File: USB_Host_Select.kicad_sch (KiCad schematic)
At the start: 9 parts, among them J10 USB_C_Receptacle_USB2.0_16P, J11 USB_C_Receptacle_USB2.0_16P, U3 TS3USB221AQRSERQ1, U7 USBLC6-2SC6, U8 USBLC6-2SC6

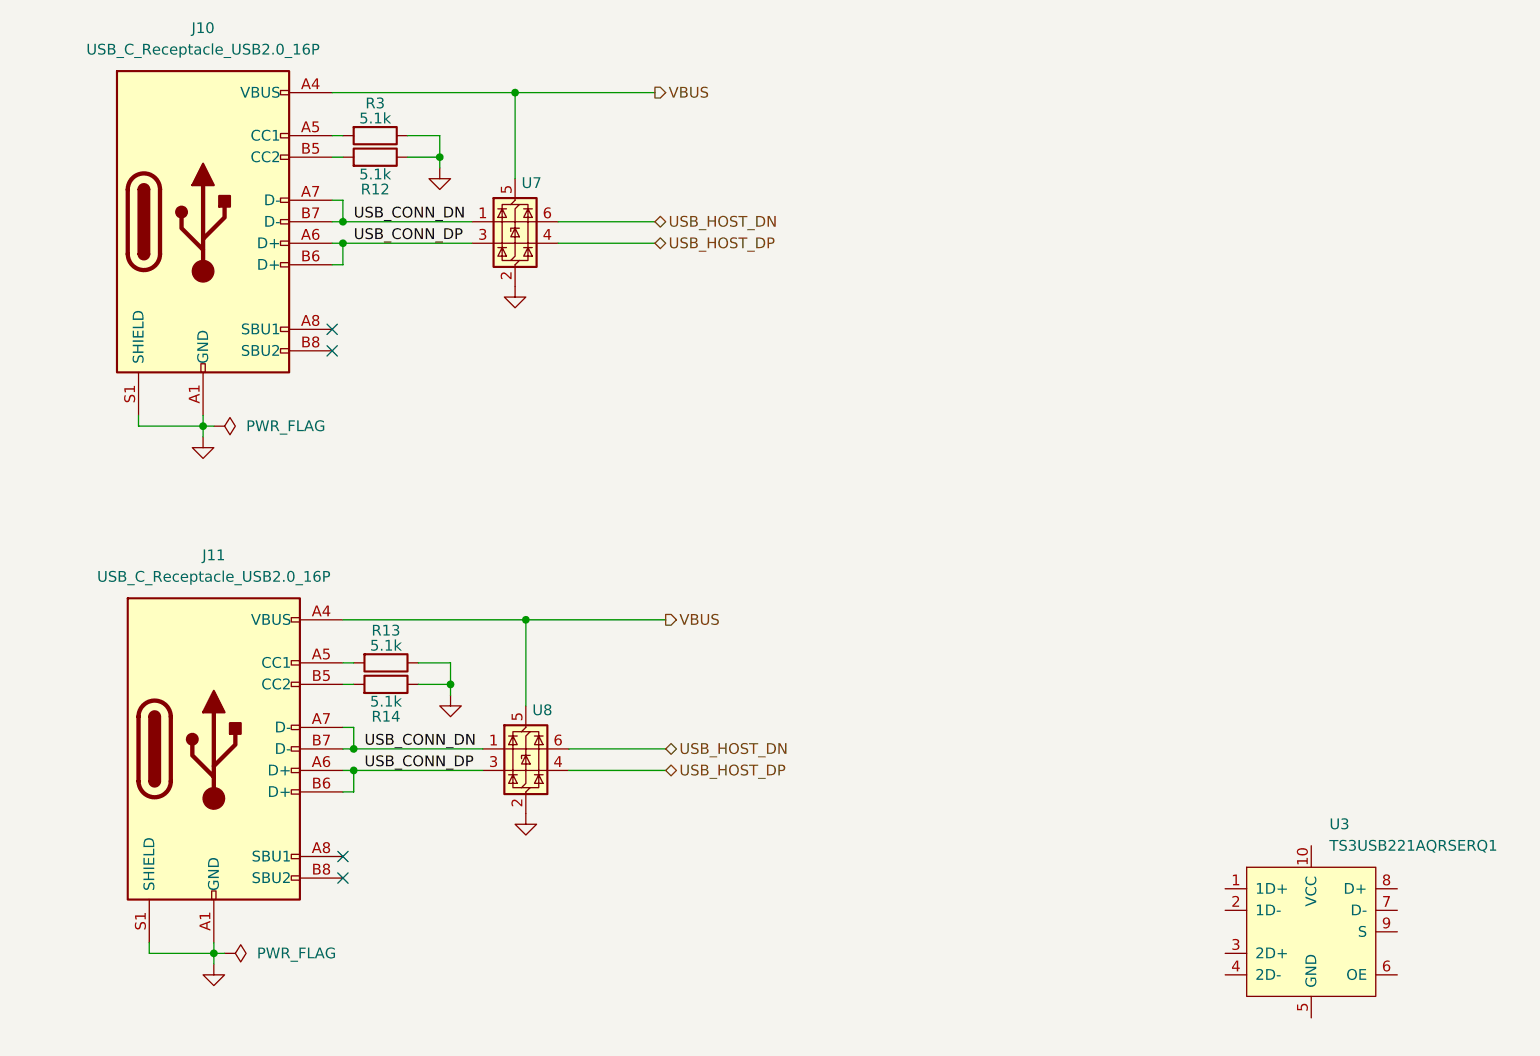
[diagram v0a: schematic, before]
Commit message: Better schematics structure & Hub sub-circuit connections
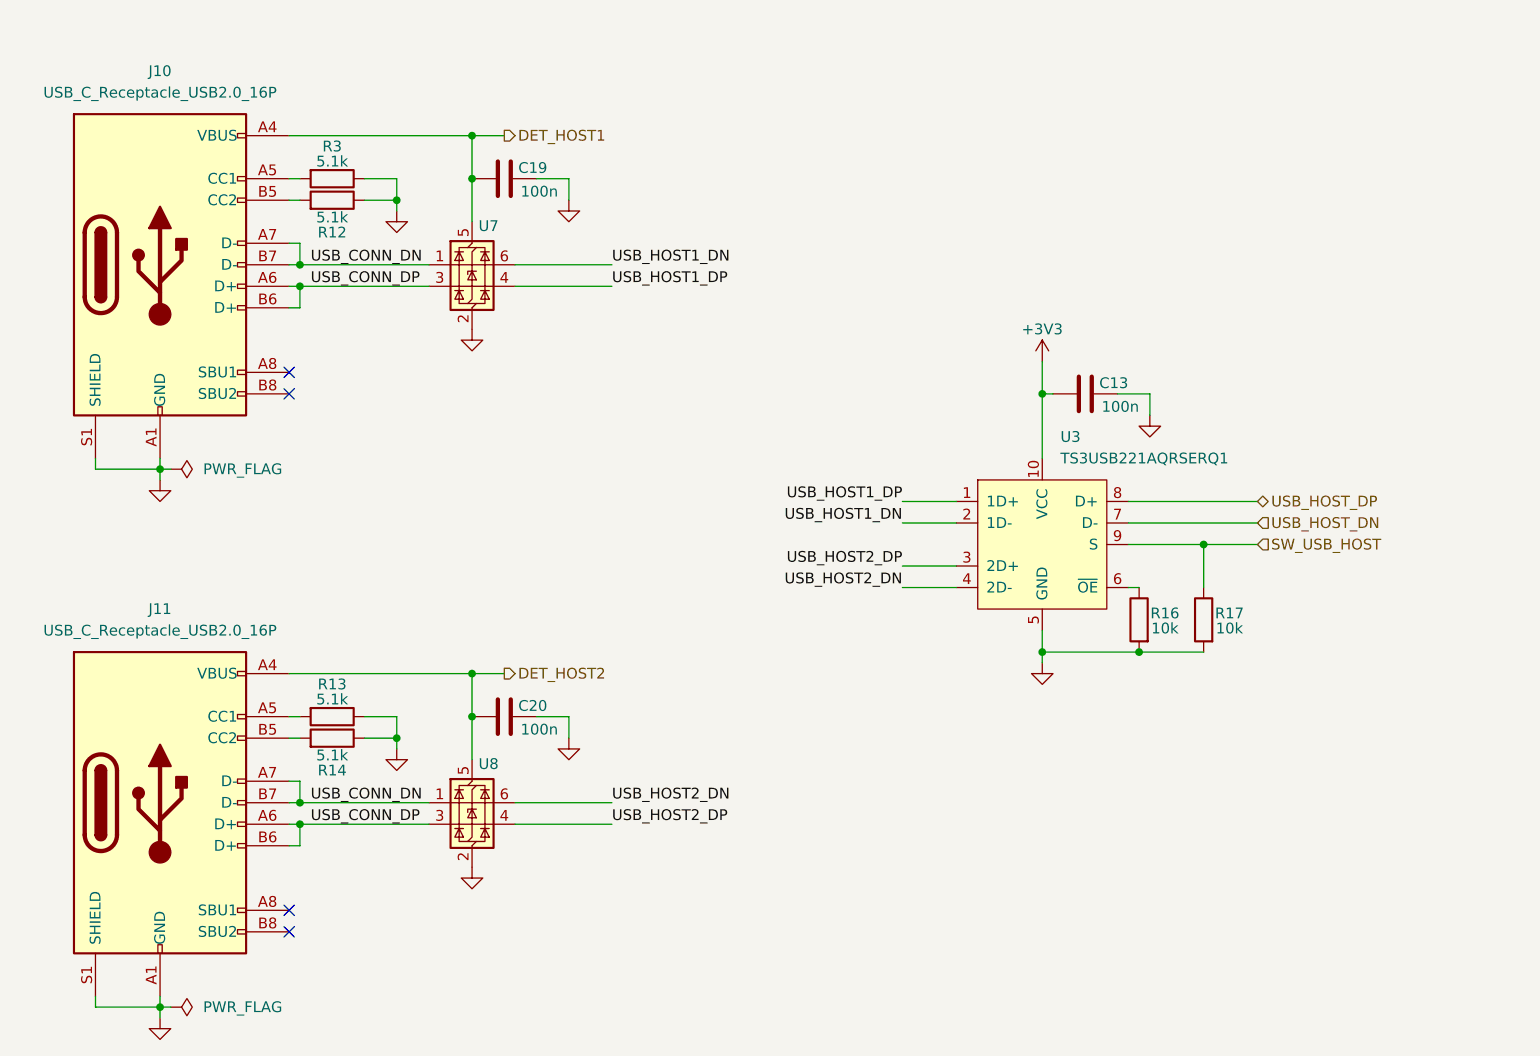
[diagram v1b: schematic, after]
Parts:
- added C13, C19, C20: 100n, Capacitor_SMD:C_0603_1608Metric, symbol Device:C
- added R16, R17: 10k, Resistor_SMD:R_0603_1608Metric, symbol Device:R
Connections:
- net GND: now also U3.5 (GND), C13.2, C19.2, C20.2, R16.2, R17.2
- net USB_HOST_DN: now also U3.7 (D-); no longer U7.6 (I/O1), U8.6 (I/O1)
- net USB_HOST_DP: now also U3.8 (D+); no longer U7.4 (I/O2), U8.4 (I/O2)
- net USB_HOST1_DP: now reaches U3.1 (1D+)
- net USB_HOST1_DP: now also U7.4 (I/O2)
- net +3V3: now reaches U3.10 (VCC)
- net +3V3: now also C13.1
- net USB_HOST1_DN: now reaches U3.2 (1D-)
- net USB_HOST1_DN: now also U7.6 (I/O1)
- net USB_HOST2_DP: now reaches U3.3 (2D+)
- net USB_HOST2_DP: now also U8.4 (I/O2)
- net USB_HOST2_DN: now reaches U3.4 (2D-)
- net USB_HOST2_DN: now also U8.6 (I/O1)
- net at U3.6 (~{OE}): now also R16.1
- net SW_USB_HOST: now reaches U3.9 (S)
- net SW_USB_HOST: now also R17.1
- net VBUS renamed DET_HOST1
- net DET_HOST1: now also C19.1; no longer J11.A4 (VBUS), J11.A9 (VBUS), J11.B4 (VBUS), J11.B9 (VBUS), U8.5 (VBUS)
- new net DET_HOST2: C20.1, J11.A4 (VBUS), J11.A9 (VBUS), J11.B4 (VBUS), J11.B9 (VBUS), U8.5 (VBUS)
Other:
- moved on the sheet: J10, J11, R12, R13, R14, R3, U3, U7, U8

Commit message: Updated symbols' DigiKey part no.
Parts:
- U3: DigiKey (none) -> 296-27719-1-ND
- U7, U8: DigiKey 4518-USBLC6-2SC6CT-ND -> 5399-USBLC6-2SC6CT-ND
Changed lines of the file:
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@@
 			)
 		)
-		(property "DigiKey" "4518-USBLC6-2SC6CT-ND"
+		(property "DigiKey" "5399-USBLC6-2SC6CT-ND"
 			(at 97.79 132.08 0)
 			(hide yes)
@@
 			)
 		)
-		(property "DigiKey" "4518-USBLC6-2SC6CT-ND"
+		(property "DigiKey" "5399-USBLC6-2SC6CT-ND"
 			(at 97.79 68.58 0)
 			(hide yes)
@@
 			(at 165.1 101.6 0)
 			(hide yes)
+			(show_name no)
+			(do_not_autoplace no)
+			(effects
+				(font
+					(size 1.27 1.27)
+				)
+			)
+		)
+		(property "DigiKey" "296-27719-1-ND"
+			(at 165.1 101.6 0)
+			(hide yes)

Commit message: Changed MCU & Stared routing HDMI connectiors
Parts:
- C14: renamed from C19; AX (none) -> 27012; AX no. 27012 -> (none)
- C15: renamed from C20; AX (none) -> 27012; AX no. 27012 -> (none)
- C16: renamed from C13; AX (none) -> 27012; AX no. 27012 -> (none)
- J2: renamed from J10; Name USB4105-GF-A -> (none)
- J3: renamed from J11; Name USB4105-GF-A -> (none)
- R10: renamed from R3; Name RC0603FR-075K1L -> (none)
- R11: renamed from R12; Name RC0603FR-075K1L -> (none)
- R12: renamed from R13; Name RC0603FR-075K1L -> (none)
- R13: renamed from R14; Name RC0603FR-075K1L -> (none)
- R14: renamed from R16; footprint Resistor_SMD:R_0603_1608Metric -> Resistor_SMD:R_0402_1005Metric; AX (none) -> 201002; AX no. 141002 -> (none)
- R15: renamed from R17; footprint Resistor_SMD:R_0603_1608Metric -> Resistor_SMD:R_0402_1005Metric; AX (none) -> 201002; AX no. 141002 -> (none)
- U4: renamed from U7; Name USBLC6-2SC6 -> (none)
- U5: renamed from U8; Name USBLC6-2SC6 -> (none)
- renumbered U3 to U6

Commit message: HDMI schematics
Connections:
- net SW_USB_HOST renamed SW
- net USB_CONN_DN renamed USB_CONN_A_DN
- net USB_CONN_A_DN: no longer J3.A7 (D-), J3.B7 (D-), U5.1 (I/O1)
- net USB_CONN_DP renamed USB_CONN_A_DP
- net USB_CONN_A_DP: no longer J3.A6 (D+), J3.B6 (D+), U5.3 (I/O2)
- net USB_HOST1_DN renamed USB_A_DN
- net USB_HOST1_DP renamed USB_A_DP
- net USB_HOST2_DN renamed USB_B_DN
- net USB_HOST2_DP renamed USB_B_DP
- new net USB_CONN_B_DN: J3.A7 (D-), J3.B7 (D-), U5.1 (I/O1)
- new net USB_CONN__BDP: J3.A6 (D+), J3.B6 (D+), U5.3 (I/O2)
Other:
- note added: "S LOW => 1D+/- = D+/-"
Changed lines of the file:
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@@
 		(rev "A")
+	)
+	(text "S LOW => 1D+/- = D+/-"
+		(exclude_from_sim no)
+		(at 203.708 106.426 0)
+		(effects
+			(font
+				(size 1.27 1.27)
+			)
+		)
 	)
 	(junction
@@
 	(wire
 		(pts
+			(xy 165.1 80.01) (xy 165.1 83.82)
+		)
+		(stroke
+			(width 0)
+			(type default)
+		)
+	)
+	(wire
+		(pts
+			(xy 77.47 73.66) (xy 76.2 73.66)
+		)
+		(stroke
+			(width 0)
+			(type default)
+		)
+	)
+	(wire
+		(pts
 			(xy 77.47 134.62) (xy 92.71 134.62)
 		)
@@
 	(wire
 		(pts
-			(xy 165.1 80.01) (xy 165.1 83.82)
-		)
-		(stroke
-			(width 0)
-			(type default)
-		)
-	)
-	(wire
-		(pts
-			(xy 77.47 73.66) (xy 76.2 73.66)
-		)
-		(stroke
-			(width 0)
-			(type default)
-		)
-	)
-	(wire
-		(pts
 			(xy 85.09 60.96) (xy 88.9 60.96)
 		)
@@
 		)
 	)
-	(label "USB_HOST1_DP"
+	(label "USB_A_DP"
 		(at 148.59 96.52 180)
 		(effects
@@
 		)
 	)
-	(label "USB_HOST2_DN"
+	(label "USB_B_DN"
 		(at 114.3 132.08 0)
 		(effects
@@
 		)
 	)
-	(label "USB_HOST2_DP"
+	(label "USB_B_DP"
 		(at 114.3 134.62 0)
 		(effects
@@
 		)
 	)
-	(label "USB_CONN_DN"
-		(at 78.74 68.58 0)
+	(label "USB_CONN_A_DN"
+		(at 77.47 68.58 0)
 		(effects
 			(font
@@
 		)
 	)
-	(label "USB_HOST1_DN"
+	(label "USB_A_DN"
 		(at 114.3 68.58 0)
 		(effects
@@
 		)
 	)
-	(label "USB_CONN_DP"
-		(at 78.74 134.62 0)
+	(label "USB_CONN__BDP"
+		(at 77.47 134.62 0)
 		(effects
 			(font
@@
 		)
 	)
-	(label "USB_HOST2_DN"
+	(label "USB_B_DN"
 		(at 148.59 106.68 180)
 		(effects
@@
 		)
 	)
-	(label "USB_HOST1_DN"
+	(label "USB_A_DN"
 		(at 148.59 99.06 180)
 		(effects
@@
 		)
 	)
-	(label "USB_HOST1_DP"
+	(label "USB_A_DP"
 		(at 114.3 71.12 0)
 		(effects
@@
 		)
 	)
-	(label "USB_HOST2_DP"
+	(label "USB_B_DP"
 		(at 148.59 104.14 180)
 		(effects
@@
 		)
 	)
-	(label "USB_CONN_DN"
-		(at 78.74 132.08 0)
+	(label "USB_CONN_B_DN"
+		(at 77.47 132.08 0)
 		(effects
 			(font
@@
 		)
 	)
-	(label "USB_CONN_DP"
-		(at 78.74 71.12 0)
+	(label "USB_CONN_A_DP"
+		(at 77.47 71.12 0)
 		(effects
 			(font
@@
 		)
 	)
-	(hierarchical_label "SW_USB_HOST"
+	(hierarchical_label "SW"
 		(shape input)
 		(at 190.5 101.6 0)

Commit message: Schematics done
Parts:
- removed C14, C15, C16: 100n, Capacitor_SMD:C_0603_1608Metric, symbol Device:C
- added C28, C30, C31: 1u, Capacitor_SMD:C_0402_1005Metric, symbol Device:C
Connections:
- net +3V3: now also C28.1
- net GND: now also C28.2, C30.2, C31.2
- net DET_HOST1: no longer names the net of J2.A4 (VBUS), J2.A9 (VBUS), J2.B4 (VBUS), J2.B9 (VBUS), U4.5 (VBUS)
- net DET_HOST1: now also C30.1
- net DET_HOST2: no longer names the net of J3.A4 (VBUS), J3.A9 (VBUS), J3.B4 (VBUS), J3.B9 (VBUS), U5.5 (VBUS)
- net DET_HOST2: now also C31.1
- net USB_HOST_DN renamed USB_UP_DN
- net USB_HOST_DP renamed USB_UP_DP

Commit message: Fixed DRC & Adnotations
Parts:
- renumbered C30 to C1, C28 to C2, C31 to C3, J2 to J1, J3 to J2, R10 to R1, R11 to R2, R14 to R3, R15 to R4, R12 to R5, R13 to R6, U4 to U1, U6 to U2, U5 to U3
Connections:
- net GND: now also J1.SH (SHIELD), J2.SH (SHIELD); no longer J1.S1 (SHIELD), J2.S1 (SHIELD)

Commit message: Updated library structure
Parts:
- removed U2: TS3USB221AQRSERQ1, TS3USB221AQRSERQ1:TS3USB221AQRSERQ1, symbol TS3USB221AQRSERQ1:TS3USB221AQRSERQ1
- added U2: TS3USB221AQRSERQ1, TS3USB221AQRSERQ1:TS3USB221AQRSERQ1, symbol Symbols:TS3USB221AQRSERQ1
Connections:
- net +3V3: now also U2.10 (VCC)
- net GND: now also U2.5 (GND)
- net SW: now also U2.9 (S)
- net USB_A_DN: now also U2.2 (1D-)
- net USB_A_DP: now also U2.1 (1D+)
- net USB_B_DN: now also U2.4 (2D-)
- net USB_B_DP: now also U2.3 (2D+)
- net USB_UP_DN: now also U2.7 (D-)
- net USB_UP_DP: now also U2.8 (D+)
- net at R3.1: now also U2.6 (~{OE})
- net USB_CONN__BDP renamed USB_CONN_B_DP
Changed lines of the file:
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@@
 		)
 	)
-	(label "USB_CONN__BDP"
+	(label "USB_CONN_B_DP"
 		(at 77.47 134.62 0)
 		(effects
@@
 	)
 	(symbol
+		(lib_id "Symbols:TS3USB221AQRSERQ1")
+		(at 165.1 101.6 0)
+		(unit 1)
+		(body_style 1)
+		(exclude_from_sim no)
+		(in_bom yes)
+		(on_board yes)
+		(in_pos_files yes)
+		(dnp no)
+		(fields_autoplaced yes)
+		(property "Reference" "U2"
+			(at 167.2433 88.9 0)
+			(show_name no)
+			(do_not_autoplace no)
+			(effects
+				(font
+					(size 1.27 1.27)
+				)
+				(justify left)
+			)
+		)
+		(property "Value" "TS3USB221AQRSERQ1"
+			(at 167.2433 91.44 0)
+			(show_name no)
+			(do_not_autoplace no)
+			(effects
+				(font
+					(size 1.27 1.27)
+				)
+				(justify left)
+			)
+		)
+		(property "Footprint" "TS3USB221AQRSERQ1:TS3USB221AQRSERQ1"
+			(at 165.1 101.6 0)
+			(hide yes)
+			(show_name no)
+			(do_not_autoplace no)
+			(effects
+				(font
+					(size 1.27 1.27)
+				)
+			)
+		)
+		(property "Datasheet" "https://www.ti.com/lit/ds/scds300e/scds300e.pdf"
+			(at 165.1 101.6 0)
+			(hide yes)
+			(show_name no)
+			(do_not_autoplace no)
+			(effects
+				(font
+					(size 1.27 1.27)
+				)
+			)
+		)
+		(property "Description" "Automotive ESD protected high-speed USB 2.0 1:2 multiplexer/demultiplexer switch"
+			(at 165.1 101.6 0)
+			(hide yes)
+			(show_name no)
+			(do_not_autoplace no)
+			(effects
+				(font
+					(size 1.27 1.27)
+				)
+			)
+		)
+		(property "DigiKey" "296-27719-1-ND"
+			(at 165.1 101.6 0)
+			(hide yes)
+			(show_name no)
+			(do_not_autoplace no)
+			(effects
+				(font
+					(size 1.27 1.27)
+				)
+			)
+		)
+		(pin "3"
+		)
+		(pin "2"
+		)
+		(pin "1"
+		)
+		(pin "9"
+		)
+		(pin "10"
+		)
+		(pin "6"
+		)
+		(pin "8"
+		)
+		(pin "7"
+		)
+		(pin "5"
+		)
+		(pin "4"
+		)
+		(instances
+			(project "KVM_Switch"
+				(path "/94386106-ccd4-487f-b5c5-d52ec3dd59db/e397aa06-0b86-4196-a73c-4d06e82b65f2"
+					(reference "U2")
+					(unit 1)
+				)
+			)
+		)
+	)
+	(symbol
 		(lib_id "power:GND")
 		(at 88.9 62.23 0)
@@
 					(unit 1)
 				)
-			)
-		)
-	)
-	(symbol
-		(lib_id "TS3USB221AQRSERQ1:TS3USB221AQRSERQ1")
-		(at 165.1 101.6 0)
-		(unit 1)
-		(body_style 1)
-		(exclude_from_sim no)
-		(in_bom yes)
-		(on_board yes)
-		(in_pos_files yes)
-		(dnp no)
-		(fields_autoplaced yes)
-		(property "Reference" "U2"
-			(at 167.2433 88.9 0)
-			(show_name no)
-			(do_not_autoplace no)
-			(effects
-				(font
-					(size 1.27 1.27)
-				)
-				(justify left)
-			)
-		)
-		(property "Value" "TS3USB221AQRSERQ1"
-			(at 167.2433 91.44 0)
-			(show_name no)
-			(do_not_autoplace no)
-			(effects
-				(font
-					(size 1.27 1.27)
-				)
-				(justify left)
-			)
-		)
-		(property "Footprint" "TS3USB221AQRSERQ1:TS3USB221AQRSERQ1"
-			(at 165.1 101.6 0)
-			(hide yes)
-			(show_name no)
-			(do_not_autoplace no)
-			(effects
-				(font
-					(size 1.27 1.27)
-				)
-			)
-		)
-		(property "Datasheet" "https://www.ti.com/lit/ds/scds300e/scds300e.pdf"
-			(at 165.1 101.6 0)
-			(hide yes)
-			(show_name no)
-			(do_not_autoplace no)
-			(effects
-				(font
-					(size 1.27 1.27)
-				)
-			)
-		)
-		(property "Description" "Automotive ESD protected high-speed USB 2.0 1:2 multiplexer/demultiplexer switch"
-			(at 165.1 101.6 0)
-			(hide yes)
-			(show_name no)
-			(do_not_autoplace no)
-			(effects
-				(font
-					(size 1.27 1.27)
-				)
-			)
-		)
-		(property "DigiKey" "296-27719-1-ND"
-			(at 165.1 101.6 0)
-			(hide yes)
-			(show_name no)
-			(do_not_autoplace no)
-			(effects
-				(font
-					(size 1.27 1.27)
-				)
-			)
-		)
-		(pin "9"
-		)
-		(pin "8"
-		)
-		(pin "7"
-		)
-		(pin "6"
-		)
-		(pin "5"
-		)
-		(pin "4"
-		)
-		(pin "3"
-		)
-		(pin "2"
-		)
-		(pin "1"
-		)
-		(pin "10"
-		)
-		(instances
-			(project "KVM_Switch"
-				(path "/94386106-ccd4-487f-b5c5-d52ec3dd59db/e397aa06-0b86-4196-a73c-4d06e82b65f2"
-					(reference "U2")
-					(unit 1)
-				)

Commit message: Library and Schematics Fixes
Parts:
- removed R4: 10k, Resistor_SMD:R_0402_1005Metric, symbol Device:R
- U2: footprint TS3USB221AQRSERQ1:TS3USB221AQRSERQ1 -> KVM_Swtich:TS3USB221AQRSERQ1
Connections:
- net DET_USB_B: now reaches C3.1, J2.A4 (VBUS), J2.A9 (VBUS), J2.B4 (VBUS), J2.B9 (VBUS), U3.5 (VBUS)
- net DET_USB_A: now reaches C1.1, J1.A4 (VBUS), J1.A9 (VBUS), J1.B4 (VBUS), J1.B9 (VBUS), U1.5 (VBUS)
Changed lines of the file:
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@@
-	)
-	(junction
-		(at 176.53 114.3)
-		(diameter 0)
-		(color 0 0 0 0)
 	)
 	(junction
@@
 	)
 	(junction
-		(at 184.15 101.6)
+		(at 107.95 53.34)
 		(diameter 0)
 		(color 0 0 0 0)
@@
 		(color 0 0 0 0)
 	)
+	(junction
+		(at 107.95 116.84)
+		(diameter 0)
+		(color 0 0 0 0)
+	)
 	(no_connect
 		(at 76.2 144.78)
@@
 	(wire
 		(pts
-			(xy 184.15 101.6) (xy 190.5 101.6)
-		)
-		(stroke
-			(width 0)
-			(type default)
-		)
-	)
-	(wire
-		(pts
 			(xy 76.2 60.96) (xy 77.47 60.96)
 		)
@@
 	(wire
 		(pts
+			(xy 107.95 116.84) (xy 114.3 116.84)
+		)
+		(stroke
+			(width 0)
+			(type default)
+		)
+	)
+	(wire
+		(pts
 			(xy 77.47 71.12) (xy 77.47 73.66)
 		)
@@
 	(wire
 		(pts
-			(xy 176.53 114.3) (xy 184.15 114.3)
-		)
-		(stroke
-			(width 0)
-			(type default)
-		)
-	)
-	(wire
-		(pts
-			(xy 175.26 101.6) (xy 184.15 101.6)
+			(xy 175.26 101.6) (xy 190.5 101.6)
 		)
 		(stroke
@@
 	(wire
 		(pts
+			(xy 107.95 53.34) (xy 114.3 53.34)
+		)
+		(stroke
+			(width 0)
+			(type default)
+		)
+	)
+	(wire
+		(pts
 			(xy 77.47 132.08) (xy 92.71 132.08)
 		)
@@
 		(pts
 			(xy 97.79 116.84) (xy 76.2 116.84)
-		)
-		(stroke
-			(width 0)
-			(type default)
-		)
-	)
-	(wire
-		(pts
-			(xy 184.15 101.6) (xy 184.15 106.68)
 		)
 		(stroke
@@
 			)
 			(justify left bottom)
+		)
+	)
+	(hierarchical_label "DET_USB_B"
+		(shape output)
+		(at 114.3 116.84 0)
+		(effects
+			(font
+				(size 1.27 1.27)
+			)
+			(justify left)
 		)
 	)
@@
 		(shape input)
 		(at 190.5 101.6 0)
+		(effects
+			(font
+				(size 1.27 1.27)
+			)
+			(justify left)
+		)
+	)
+	(hierarchical_label "DET_USB_A"
+		(shape output)
+		(at 114.3 53.34 0)
 		(effects
 			(font
@@
 	)
 	(symbol
-		(lib_id "Device:R")
-		(at 184.15 110.49 0)
-		(mirror y)
-		(unit 1)
-		(body_style 1)
-		(exclude_from_sim no)
-		(in_bom yes)
-		(on_board yes)
-		(in_pos_files yes)
-		(dnp no)
-		(property "Reference" "R4"
-			(at 187.198 109.728 0)
-			(show_name no)
-			(do_not_autoplace no)
-			(effects
-				(font
-					(size 1.27 1.27)
-				)
-			)
-		)
-		(property "Value" "10k"
-			(at 187.198 111.506 0)
-			(show_name no)
-			(do_not_autoplace no)
-			(effects
-				(font
-					(size 1.27 1.27)
-				)
-			)
-		)
-		(property "Footprint" "Resistor_SMD:R_0402_1005Metric"
-			(at 185.928 110.49 90)
-			(hide yes)
-			(show_name no)
-			(do_not_autoplace no)
-			(effects
-				(font
-					(size 1.27 1.27)
-				)
-			)
-		)
-		(property "Datasheet" ""
-			(at 184.15 110.49 0)
-			(hide yes)
-			(show_name no)
-			(do_not_autoplace no)
-			(effects
-				(font
-					(size 1.27 1.27)
-				)
-			)
-		)
-		(property "Description" "Resistor"
-			(at 184.15 110.49 0)
-			(hide yes)
-			(show_name no)
-			(do_not_autoplace no)
-			(effects
-				(font
-					(size 1.27 1.27)
-				)
-			)
-		)
-		(property "AX" "201002"
-			(at 184.15 110.49 0)
-			(hide yes)
-			(show_name no)
-			(do_not_autoplace no)
-			(effects
-				(font
-					(size 1.27 1.27)
-				)
-			)
-		)
-		(pin "2"
-		)
-		(pin "1"
-		)
-		(instances
-			(project "KVM_Switch"
-				(path "/94386106-ccd4-487f-b5c5-d52ec3dd59db/e397aa06-0b86-4196-a73c-4d06e82b65f2"
-					(reference "R4")
-					(unit 1)
-				)
-			)
-		)
-	)
-	(symbol
 		(lib_id "Device:C")
 		(at 107.95 121.92 0)
@@
 			)
 		)
-		(property "Footprint" "TS3USB221AQRSERQ1:TS3USB221AQRSERQ1"
+		(property "Footprint" "KVM_Swtich:TS3USB221AQRSERQ1"
 			(at 165.1 101.6 0)
 			(hide yes)
